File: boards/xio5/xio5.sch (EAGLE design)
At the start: 79 parts

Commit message: Start adding busses
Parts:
- removed U$1: ZTURN, pbxl:ZTURN
- added J1: 98424-G52-14ALF, samacsys:98424-G52-14ALF
- added JP1: (no value), pinhead:PINHD-1X7
- added ZTURN: ZTURN, pbxl:ZTURN
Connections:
- new net !SRST!: J1.B7, JP1.6, ZTURN-JTAG.!JTAG_RST!@CN1_14
- new net TCK: J1.B3, JP1.3, ZTURN-JTAG.JTAG_TCK@CN1_6
- new net TDI: J1.B5, JP1.5, ZTURN-JTAG.JTAG_TDI@CN1_10
- new net TDO: J1.B4, JP1.4, ZTURN-JTAG.JTAG_TDO@CN1_12
- new net TMS: J1.B2, JP1.2, ZTURN-JTAG.JTAG_TMS@CN1_8
- net +3V3: now also J1.B1, JP1.1, ZTURN-POWER.VDD33@CN1_3, ZTURN-POWER.VDD33@CN2_3, ZTURN-POWER.VDDIO_13_PL@CN1_15, ZTURN-POWER.VDDIO_34_PL@CN1_49, ZTURN-POWER.VDDIO_35_PL@CN2_51
- net +5V: now also ZTURN-POWER.VDD5@CN1_1, ZTURN-POWER.VDD5@CN2_1
- net GND: now also J1.A1, J1.A2, J1.A3, J1.A4, J1.A5, J1.A6, J1.A7, JP1.7, ZTURN-POWER.GND@CN1_2, ZTURN-POWER.GND@CN1_24, ZTURN-POWER.GND@CN1_25, ZTURN-POWER.GND@CN1_34, ZTURN-POWER.GND@CN1_35, ZTURN-POWER.GND@CN1_4, ZTURN-POWER.GND@CN1_44, ZTURN-POWER.GND@CN1_54, ZTURN-POWER.GND@CN1_67, ZTURN-POWER.GND@CN1_68, ZTURN-POWER.GND@CN2_2, ZTURN-POWER.GND@CN2_20, ZTURN-POWER.GND@CN2_21, ZTURN-POWER.GND@CN2_30, ZTURN-POWER.GND@CN2_31, ZTURN-POWER.GND@CN2_4, ZTURN-POWER.GND@CN2_40, ZTURN-POWER.GND@CN2_41, ZTURN-POWER.GND@CN2_50, ZTURN-POWER.GND@CN2_60, ZTURN-POWER.GND@CN2_61, ZTURN-POWER.GND@CN2_70, ZTURN-POWER.GND@CN2_71, ZTURN-POWER.GND@CN2_80
- net LO_A0: now also ZTURN-CN2.IO_B35_LN15@CN2_59
- net LO_A1: now also ZTURN-CN2.IO_B35_LP15@CN2_57
- net LO_A10: now also ZTURN-CN2.IO_B35_LN5@CN2_35
- net LO_A11: now also ZTURN-CN2.IO_B35_LP5@CN2_33
- net LO_A12: now also ZTURN-CN2.IO_B35_LN3@CN2_29
- net LO_A13: now also ZTURN-CN2.IO_B35_LP3@CN2_27
- net LO_A14: now also ZTURN-CN2.IO_B35_LN1@CN2_25
- net LO_A15: now also ZTURN-CN2.IO_B35_LP1@CN2_23
- net LO_A2: now also ZTURN-CN2.IO_B35_LN13@CN2_55
- net LO_A3: now also ZTURN-CN2.IO_B35_LP13@CN2_53
- net LO_A4: now also ZTURN-CN2.IO_B35_LN11@CN2_49
- net LO_A5: now also ZTURN-CN2.IO_B35_LP11@CN2_47
- net LO_A6: now also ZTURN-CN2.IO_B35_LN9@CN2_45
- net LO_A7: now also ZTURN-CN2.IO_B35_LP9@CN2_43
- net LO_A8: now also ZTURN-CN2.IO_B35_LN7@CN2_39
- net LO_A9: now also ZTURN-CN2.IO_B35_LP7@CN2_37
- net LO_D0: now also ZTURN-CN2.IO_B35_LN23@CN2_79
- net LO_D1: now also ZTURN-CN2.IO_B35_LP23@CN2_77
- net LO_D2: now also ZTURN-CN2.IO_B35_LN21@CN2_75
- net LO_D3: now also ZTURN-CN2.IO_B35_LP21@CN2_73
- net LO_D4: now also ZTURN-CN2.IO_B35_LN19@CN2_69
- net LO_D5: now also ZTURN-CN2.IO_B35_LP19@CN2_67
- net LO_D6: now also ZTURN-CN2.IO_B35_LN17@CN2_65
- net LO_D7: now also ZTURN-CN2.IO_B35_LP17@CN2_63
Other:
- note added: "Power, JTAG, unused"
- note removed: "SD Card"

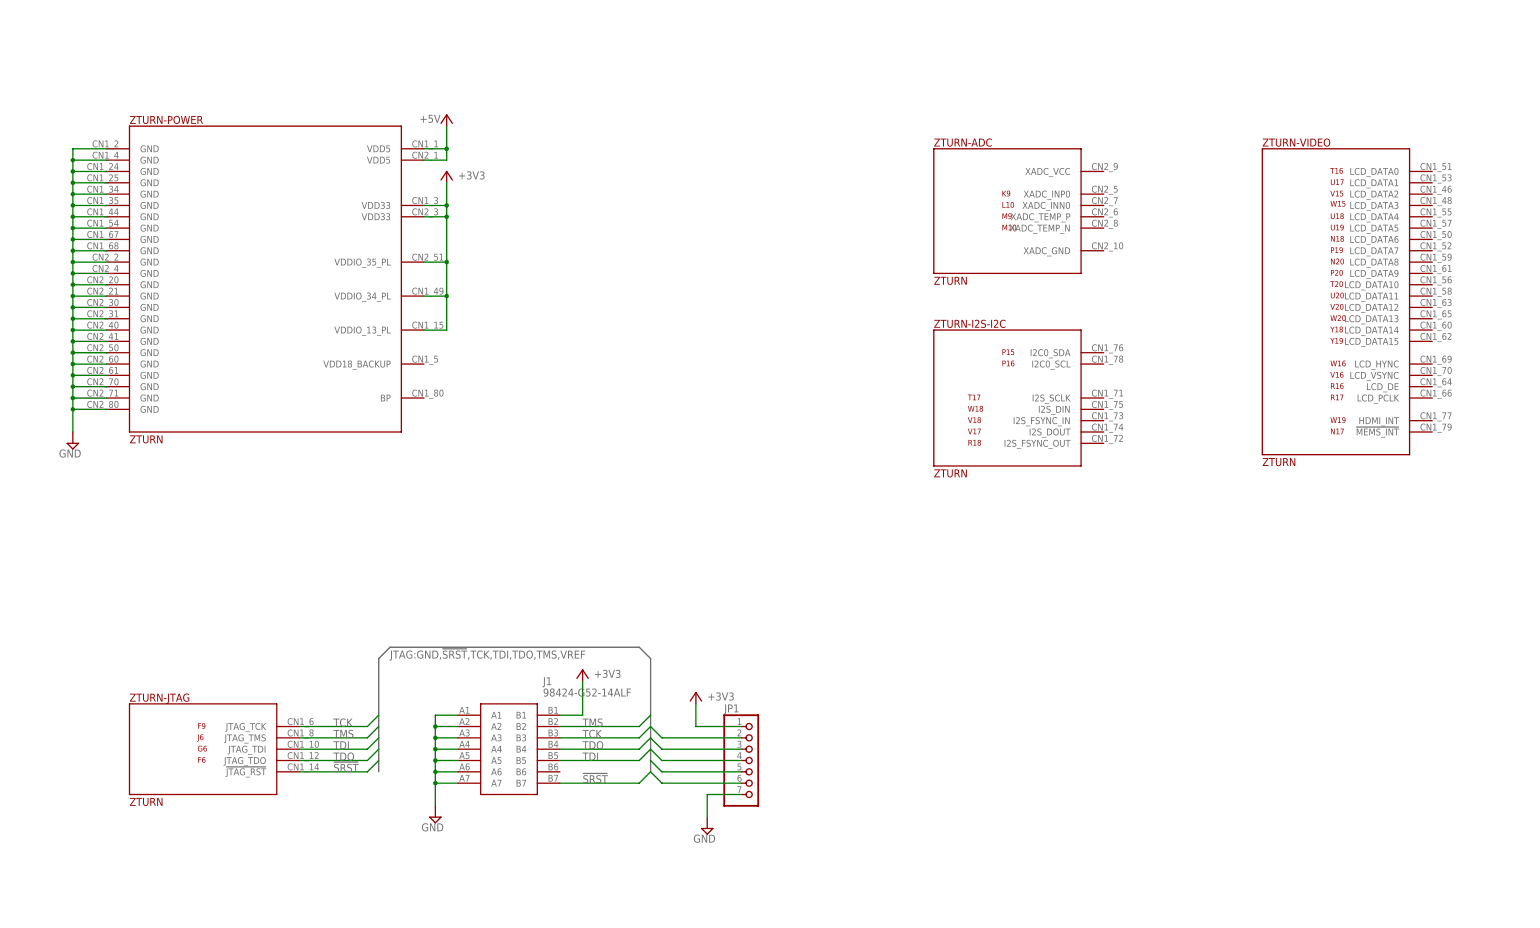
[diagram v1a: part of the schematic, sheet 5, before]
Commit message: Reorganise slot signals (ZBUS) and add the internal slot expansion interface (XBUS)
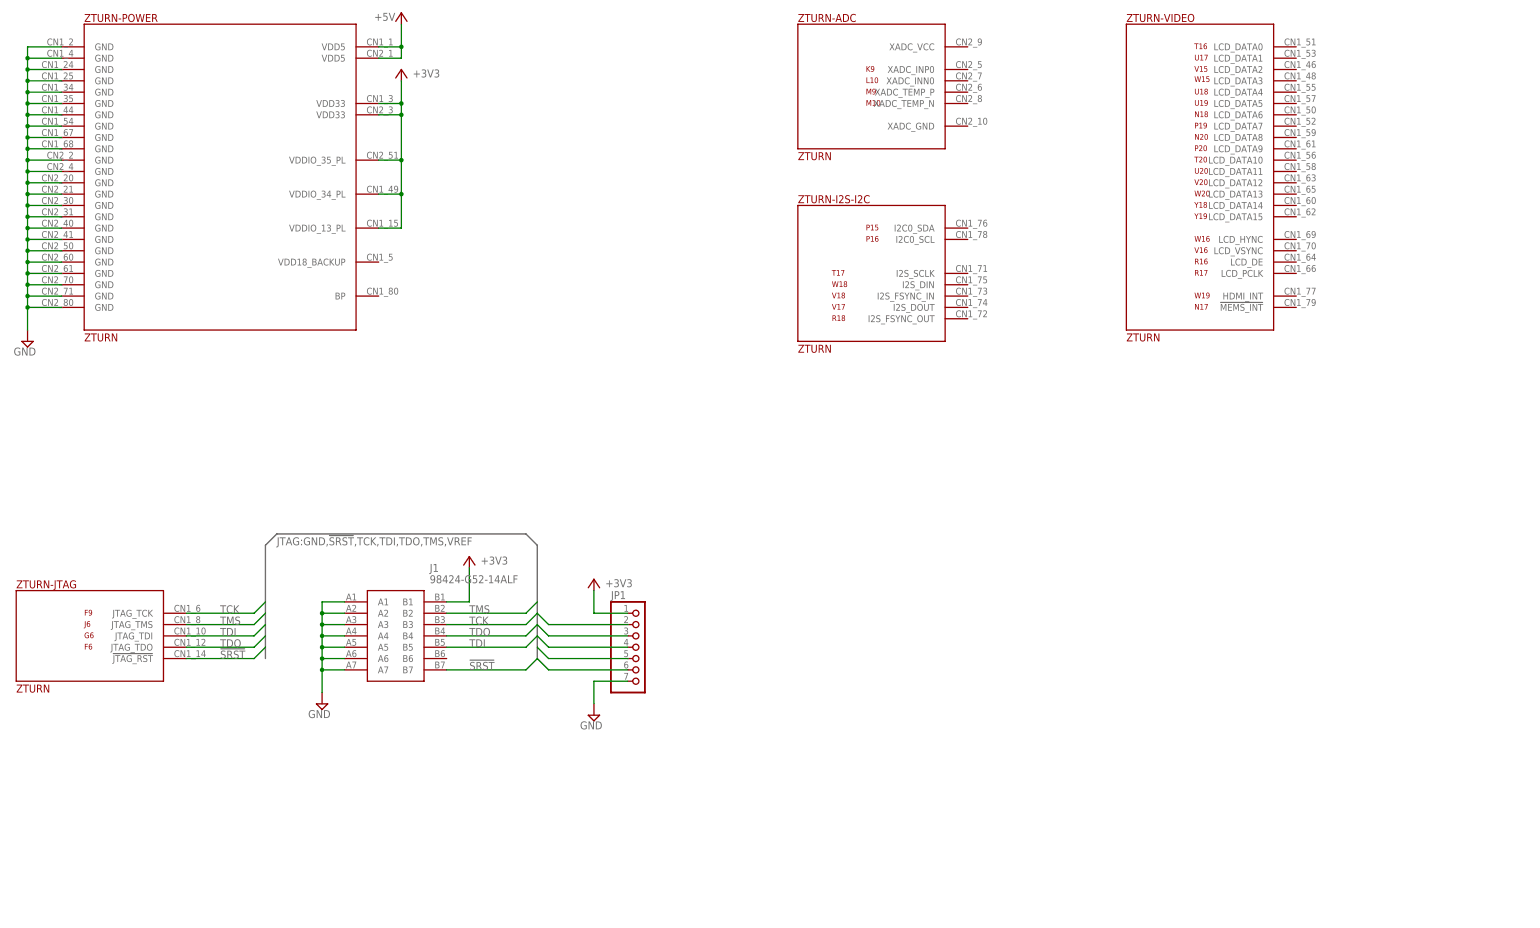
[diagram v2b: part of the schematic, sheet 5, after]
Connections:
- removed net !LO_CCTL!: SLOT0.A27, SLOT1.A27, SLOT2.A27, SLOT3.A27, SLOT4.A27
- removed net !LO_REF!: SLOT0.B15, SLOT1.B15, SLOT2.B15, SLOT3.B15, SLOT4.B15
- removed net HBUS0: SLOT0.B18, SLOT1.B18, SLOT2.B18, SLOT3.B18, SLOT4.B18
- removed net HBUS1: SLOT0.B19, SLOT1.B19, SLOT2.B19, SLOT3.B19, SLOT4.B19
- removed net HBUS10: SLOT0.B28, SLOT1.B28, SLOT2.B28, SLOT3.B28, SLOT4.B28
- removed net HBUS11: SLOT0.B29, SLOT1.B29, SLOT2.B29, SLOT3.B29, SLOT4.B29
- removed net HBUS12: SLOT0.B30, SLOT1.B30, SLOT2.B30, SLOT3.B30, SLOT4.B30
- removed net HBUS13: SLOT0.B31, SLOT1.B31, SLOT2.B31, SLOT3.B31, SLOT4.B31
- removed net HBUS2: SLOT0.B20, SLOT1.B20, SLOT2.B20, SLOT3.B20, SLOT4.B20
- removed net HBUS3: SLOT0.B21, SLOT1.B21, SLOT2.B21, SLOT3.B21, SLOT4.B21
- removed net HBUS4: SLOT0.B22, SLOT1.B22, SLOT2.B22, SLOT3.B22, SLOT4.B22
- removed net HBUS5: SLOT0.B23, SLOT1.B23, SLOT2.B23, SLOT3.B23, SLOT4.B23
- removed net HBUS6: SLOT0.B24, SLOT1.B24, SLOT2.B24, SLOT3.B24, SLOT4.B24
- removed net HBUS7: SLOT0.B25, SLOT1.B25, SLOT2.B25, SLOT3.B25, SLOT4.B25
- removed net HBUS8: SLOT0.B26, SLOT1.B26, SLOT2.B26, SLOT3.B26, SLOT4.B26
- removed net HBUS9: SLOT0.B27, SLOT1.B27, SLOT2.B27, SLOT3.B27, SLOT4.B27
- removed net SPI0_IRQ: SLOT0.A8
- removed net SPI0_MOSI: SLOT0.A9
- removed net SPI1_IRQ: SLOT1.A8
- removed net SPI1_MISO: SLOT1.A10
- removed net SPI1_MOSI: SLOT1.A9
- removed net SPI2_IRQ: SLOT2.A8
- removed net SPI2_MISO: SLOT2.A10
- removed net SPI2_MOSI: SLOT2.A9
- removed net SPI3_IRQ: SLOT3.A8
- removed net SPI3_MISO: SLOT3.A10
- removed net SPI3_MOSI: SLOT3.A9
- removed net SPI4_IRQ: SLOT4.A8
- removed net SPI4_MISO: SLOT4.A10
- removed net SPI4_MOSI: SLOT4.A9
- removed net SPIO_MISO: SLOT0.A10
- removed net VALID_RD: SLOT0.A7, SLOT1.A7, SLOT2.A7, SLOT3.A7, SLOT4.A7
- removed net VALID_WR: SLOT0.A6, SLOT1.A6, SLOT2.A6, SLOT3.A6, SLOT4.A6
- new net !AVALID!: SLOT0.A9, SLOT1.A9, SLOT2.A9, SLOT3.A9, SLOT4.A9
- new net HSPI0_IRQ0: SLOT0.A7, ZTURN-CN2.IO_B35_LN22@CN2_74
- new net HSPI0_IRQ1: SLOT1.A7, ZTURN-CN2.IO_B35_LP22@CN2_72
- new net HSPI0_IRQ2: SLOT2.A7, ZTURN-CN2.IO_B35_LN20@CN2_68
- new net HSPI0_MISO: SLOT0.A4, SLOT1.A4, SLOT2.A4, ZTURN-CN2.IO_B35_LN24@CN2_78
- new net HSPI0_MOSI: SLOT0.A5, SLOT1.A5, SLOT2.A5, ZTURN-CN2.IO_B35_LP24@CN2_76
- new net HSPI0_SS0: SLOT0.A6, ZTURN-CN2.IO_B35_LP20@CN2_66
- new net HSPI0_SS1: SLOT1.A6, ZTURN-CN2.IO_B35_LN18@CN2_64
- new net HSPI0_SS2: SLOT2.A6, ZTURN-CN2.IO_B35_LP18@CN2_62
- new net HSPI1_IRQ0: SLOT3.A7, ZTURN-CN2.IO_B35_LN14@CN2_54
- new net HSPI1_IRQ1: SLOT4.A7, ZTURN-CN2.IO_B35_LP14@CN2_52
- new net HSPI1_IRQ2: ZTURN-CN2.IO_B35_LN10@CN2_48
- new net HSPI1_MISO: SLOT3.A4, SLOT4.A4, ZTURN-CN2.IO_B35_LN16@CN2_58
- new net HSPI1_MOSI: SLOT3.A5, SLOT4.A5, ZTURN-CN2.IO_B35_LP16@CN2_56
- new net HSPI1_SS0: SLOT3.A6, ZTURN-CN2.IO_B35_LP12@CN2_46
- new net HSPI1_SS1: SLOT4.A6, ZTURN-CN2.IO_B35_LN10@CN2_44
- new net HSPI1_SS2: ZTURN-CN2.IO_B35_LP10@CN2_42
- new net SX_PRESENT: ZTURN-CN2.IO_B35_LP4@CN2_26
- new net XBUS0: ZTURN-CN1.IO_B34_LP11@CN1_45
- new net XBUS1: ZTURN-CN1.IO_B34_LN11@CN1_47
- new net XBUS10: ZTURN-CN1.IO_B34_LP5@CN1_36
- new net XBUS11: ZTURN-CN1.IO_B34_LN5@CN1_38
- new net XBUS12: ZTURN-CN1.IO_B34_LP7@CN1_40
- new net XBUS13: ZTURN-CN1.IO_B34_LN7@CN1_42
- new net XBUS14: ZTURN-CN2.IO_B35_LP2@CN2_22
- new net XBUS15: ZTURN-CN2.IO_B35_LN2@CN2_24
- new net XBUS2: ZTURN-CN1.IO_B13_LP14@CN1_16
- new net XBUS3: ZTURN-CN1.IO_B13_LN14@CN1_18
- new net XBUS4: ZTURN-CN1.IO_B13_LP21@CN1_20
- new net XBUS5: ZTURN-CN1.IO_B13_LN21@CN1_22
- new net XBUS6: ZTURN-CN1.IO_B34_LP1@CN1_26
- new net XBUS7: ZTURN-CN1.IO_B34_LN1@CN1_28
- new net XBUS8: ZTURN-CN1.IO_B34_LP3@CN1_30
- new net XBUS9: ZTURN-CN1.IO_B34_LN3@CN1_32
- new net ZBUS0: SLOT0.B16, SLOT1.B16, SLOT2.B16, SLOT3.B16, SLOT4.B16, ZTURN-CN1.IO_B34_LN8@CN1_43
- new net ZBUS1: SLOT0.B17, SLOT1.B17, SLOT2.B17, SLOT3.B17, SLOT4.B17, ZTURN-CN1.IO_B34_LP8@CN1_41
- new net ZBUS10: SLOT0.B26, SLOT1.B26, SLOT2.B26, SLOT3.B26, SLOT4.B26, ZTURN-CN1.IO_B13_LN13@CN1_19
- new net ZBUS11: SLOT0.B27, SLOT1.B27, SLOT2.B27, SLOT3.B27, SLOT4.B27, ZTURN-CN1.IO_B13_LP13@CN1_17
- new net ZBUS12: SLOT0.B28, SLOT1.B28, SLOT2.B28, SLOT3.B28, SLOT4.B28, ZTURN-CN1.IO_B13_LN12@CN1_13
- new net ZBUS13: SLOT0.B29, SLOT1.B29, SLOT2.B29, SLOT3.B29, SLOT4.B29, ZTURN-CN1.IO_B13_P12@CN1_11
- new net ZBUS14: SLOT0.B30, SLOT1.B30, SLOT2.B30, SLOT3.B30, SLOT4.B30, ZTURN-CN1.IO_B13_LN11@CN1_9
- new net ZBUS15: SLOT0.B31, SLOT1.B31, SLOT2.B31, SLOT3.B31, SLOT4.B31, ZTURN-CN1.IO_B13_LP11@CN1_7
- new net ZBUS2: SLOT0.B18, SLOT1.B18, SLOT2.B18, SLOT3.B18, SLOT4.B18, ZTURN-CN1.IO_B34_LN6@CN1_39
- new net ZBUS3: SLOT0.B19, SLOT1.B19, SLOT2.B19, SLOT3.B19, SLOT4.B19, ZTURN-CN1.IO_B34_LP6@CN1_37
- new net ZBUS4: SLOT0.B20, SLOT1.B20, SLOT2.B20, SLOT3.B20, SLOT4.B20, ZTURN-CN1.IO_B34_LN4@CN1_33
- new net ZBUS5: SLOT0.B21, SLOT1.B21, SLOT2.B21, SLOT3.B21, SLOT4.B21, ZTURN-CN1.IO_B34_LP4@CN1_31
- new net ZBUS6: SLOT0.B22, SLOT1.B22, SLOT2.B22, SLOT3.B22, SLOT4.B22, ZTURN-CN1.IO_B34_LN2@CN1_29
- new net ZBUS7: SLOT0.B23, SLOT1.B23, SLOT2.B23, SLOT3.B23, SLOT4.B23, ZTURN-CN1.IO_B34_LP2@CN1_27
- new net ZBUS8: SLOT0.B24, SLOT1.B24, SLOT2.B24, SLOT3.B24, SLOT4.B24, ZTURN-CN1.IO_B13_LN15@CN1_23
- new net ZBUS9: SLOT0.B25, SLOT1.B25, SLOT2.B25, SLOT3.B25, SLOT4.B25, ZTURN-CN1.IO_B13_LP15@CN1_21
- net !LO_RST!: now also SLOT0.A27, SLOT1.A27, SLOT2.A27, SLOT3.A27, SLOT4.A27; no longer SLOT0.B16, SLOT1.B16, SLOT2.B16, SLOT3.B16, SLOT4.B16
- net GND: now also SLOT0.A10, SLOT0.A8, SLOT1.A10, SLOT1.A8, SLOT2.A10, SLOT2.A8, SLOT3.A10, SLOT3.A8, SLOT4.A10, SLOT4.A8; no longer SLOT0.A4, SLOT0.A5, SLOT1.A4, SLOT1.A5, SLOT2.A4, SLOT2.A5, SLOT3.A4, SLOT3.A5, SLOT4.A4, SLOT4.A5
- net LO_A10: now also ZTURN-CN2.IO_B35_LP3@CN2_27; no longer ZTURN-CN2.IO_B35_LN5@CN2_35
- net LO_A11: now also ZTURN-CN2.IO_B35_LN3@CN2_29; no longer ZTURN-CN2.IO_B35_LP5@CN2_33
- net LO_A12: now also ZTURN-CN2.IO_B35_LP5@CN2_33; no longer ZTURN-CN2.IO_B35_LN3@CN2_29
- net LO_A13: now also ZTURN-CN2.IO_B35_LN5@CN2_35; no longer ZTURN-CN2.IO_B35_LP3@CN2_27
- net LO_A14: now also ZTURN-CN2.IO_B35_LP7@CN2_37; no longer ZTURN-CN2.IO_B35_LN1@CN2_25
- net LO_A15: now also ZTURN-CN2.IO_B35_LN7@CN2_39; no longer ZTURN-CN2.IO_B35_LP1@CN2_23
- net LO_A8: now also ZTURN-CN2.IO_B35_LP1@CN2_23; no longer ZTURN-CN2.IO_B35_LN7@CN2_39
- net LO_A9: now also ZTURN-CN2.IO_B35_LN1@CN2_25; no longer ZTURN-CN2.IO_B35_LP7@CN2_37
- net LO_R/!W!: now also SLOT0.B15, SLOT1.B15, SLOT2.B15, SLOT3.B15, SLOT4.B15; no longer SLOT0.B17, SLOT1.B17, SLOT2.B17, SLOT3.B17, SLOT4.B17
- net S0_PRESENT: now also ZTURN-CN2.IO_B35_LN8@CN2_38
- net S1_PRESENT: now also ZTURN-CN2.IO_B35_LP8@CN2_36
- net S2_PRESENT: now also ZTURN-CN2.IO_B35_LN6@CN2_34
- net S3_PRESENT: now also ZTURN-CN2.IO_B35_LP6@CN2_32
- net S4_PRESENT: now also ZTURN-CN2.IO_B35_LN4@CN2_28
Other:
- note added: "!ADDR_VALID!"
- note added: "!PRESENT! x5"
- note added: "Zynq 7020 CGA400"
- note removed: "!ADDR_VALID_READ!"
- note removed: "!ADDR_VALID_WRITE!"
- note removed: "/7"
- note removed: "Artix 7 XC7A35T-1 BGA256"
- moved on the sheet: C55, J1, JP1, LD_2P, R101, R63, SLOT2, ZTURN-ADC, ZTURN-I2S-I2C, ZTURN-JTAG, ZTURN-POWER, ZTURN-VIDEO

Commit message: Work on some of the internal expansion stuff
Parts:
- added C19: 0.1uF, rcl:C-EUC0201
- added IC1: PCAL6416APW,118, samacsys:PCAL6416APW,118
- added JP2: (no value), pinhead:PINHD-2X2
- added JP3: (no value), pinhead-2:PINHD-2X16_2.00
- added LD_M0, LD_M1: Orange, led:LEDCHIPLED_0603
- added R1, R6: 59R, rcl:R-EU_R0402
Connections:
- removed net XBUS0: ZTURN-CN1.IO_B34_LP11@CN1_45
- removed net XBUS1: ZTURN-CN1.IO_B34_LN11@CN1_47
- removed net XBUS10: ZTURN-CN1.IO_B34_LP5@CN1_36
- removed net XBUS11: ZTURN-CN1.IO_B34_LN5@CN1_38
- removed net XBUS12: ZTURN-CN1.IO_B34_LP7@CN1_40
- removed net XBUS13: ZTURN-CN1.IO_B34_LN7@CN1_42
- removed net XBUS14: ZTURN-CN2.IO_B35_LP2@CN2_22
- removed net XBUS15: ZTURN-CN2.IO_B35_LN2@CN2_24
- removed net XBUS2: ZTURN-CN1.IO_B13_LP14@CN1_16
- removed net XBUS3: ZTURN-CN1.IO_B13_LN14@CN1_18
- removed net XBUS4: ZTURN-CN1.IO_B13_LP21@CN1_20
- removed net XBUS5: ZTURN-CN1.IO_B13_LN21@CN1_22
- removed net XBUS6: ZTURN-CN1.IO_B34_LP1@CN1_26
- removed net XBUS7: ZTURN-CN1.IO_B34_LN1@CN1_28
- removed net XBUS8: ZTURN-CN1.IO_B34_LP3@CN1_30
- removed net XBUS9: ZTURN-CN1.IO_B34_LN3@CN1_32
- new net N$2: IC1.P0_7, R6.2
- new net N$3: LD_M1.A, R6.1
- new net N$4: IC1.!INT, ZTURN-CN2.IO_B35_LP8@CN2_36
- new net N$5: IC1.!RESET, ZTURN-CN2.IO_B35_LN8@CN2_38
- new net N$7: IC1.P0_6, R1.2
- new net N$8: LD_M0.A, R1.1
- new net SCL: IC1.SCL, JP2.2, ZTURN-I2S-I2C.I2C0_SCL@CN1_78
- new net SDA: IC1.SDA, JP2.4, ZTURN-I2S-I2C.I2C0_SDA@CN1_76
- new net XIO0: IC1.P1_0, JP3.13
- new net XIO1: IC1.P1_1, JP3.15
- new net XIO2: IC1.P1_2, JP3.17
- new net XIO3: IC1.P1_3, JP3.19
- new net XIO4: IC1.P1_4, JP3.21
- new net XIO5: IC1.P1_5, JP3.23
- new net XIO6: IC1.P1_6, JP3.25
- new net XIO7: IC1.P1_7, JP3.27
- new net XSPI_IRQ: JP3.5, ZTURN-CN2.IO_B35_LN4@CN2_28
- new net XSPI_MISO: JP2.1, JP3.7, ZTURN-CN2.IO_B35_LP6@CN2_32
- new net XSPI_MOSI: JP2.3, JP3.9, ZTURN-CN2.IO_B35_LN6@CN2_34
- net !LO_EXTSEL!: now also ZTURN-CN1.IO_B34_LN3@CN1_32
- net !LO_HALT!: now also ZTURN-CN1.IO_B34_LP5@CN1_36
- net !LO_IRQ!: now also ZTURN-CN1.IO_B34_LN5@CN1_38
- net !LO_MPD!: now also ZTURN-CN1.IO_B34_LP7@CN1_40
- net !LO_RST!: now also ZTURN-CN2.IO_B35_LN2@CN2_24
- net +3V3: now also C19.1, IC1.VDD(I2C-BUS), IC1.VDD(P)
- net +5V: now also JP3.1, JP3.3
- net DIR_A: now also ZTURN-CN1.IO_B34_LP11@CN1_45
- net DIR_CLK: no longer U$15.DIR@5
- net DIR_D: now also ZTURN-CN1.IO_B34_LN11@CN1_47
- net DIR_EXTSEL: now also ZTURN-CN1.IO_B13_LP14@CN1_16
- net DIR_HALT: now also ZTURN-CN1.IO_B13_LN14@CN1_18
- net DIR_IRQ: now also ZTURN-CN1.IO_B13_LP21@CN1_20
- net DIR_MPD: now also ZTURN-CN1.IO_B13_LN21@CN1_22
- net DIR_RD4: no longer U$16.DIR@5
- net DIR_RD5: no longer U$14.DIR@5
- net DIR_RST: now also ZTURN-CN1.IO_B34_LP1@CN1_26
- net DIR_RW: now also ZTURN-CN1.IO_B34_LN1@CN1_28
- net GND: now also C19.2, IC1.ADDR, IC1.VSS, JP3.29, JP3.31, LD_M0.C, LD_M1.C, U$14.DIR@5, U$15.DIR@5, U$16.DIR@5
- net LO_CLK: now also ZTURN-CN1.IO_B34_LP3@CN1_30
- net LO_R/!W!: now also ZTURN-CN2.IO_B35_LP4@CN2_26
- net LO_RD4: now also ZTURN-CN1.IO_B34_LN7@CN1_42
- net LO_RD5: now also ZTURN-CN2.IO_B35_LP2@CN2_22
- net S0_PRESENT: now also IC1.P0_0; no longer ZTURN-CN2.IO_B35_LN8@CN2_38
- net S1_PRESENT: now also IC1.P0_1; no longer ZTURN-CN2.IO_B35_LP8@CN2_36
- net S2_PRESENT: now also IC1.P0_2; no longer ZTURN-CN2.IO_B35_LN6@CN2_34
- net S3_PRESENT: now also IC1.P0_3; no longer ZTURN-CN2.IO_B35_LP6@CN2_32
- net S4_PRESENT: now also IC1.P0_4; no longer ZTURN-CN2.IO_B35_LN4@CN2_28
- net SX_PRESENT: now also IC1.P0_5, JP3.11; no longer ZTURN-CN2.IO_B35_LP4@CN2_26
- net ZBUS0: now also JP3.32
- net ZBUS1: now also JP3.30
- net ZBUS10: now also JP3.12
- net ZBUS11: now also JP3.10
- net ZBUS12: now also JP3.8
- net ZBUS13: now also JP3.6
- net ZBUS14: now also JP3.4
- net ZBUS15: now also JP3.2
- net ZBUS2: now also JP3.28
- net ZBUS3: now also JP3.26
- net ZBUS4: now also JP3.24
- net ZBUS5: now also JP3.22
- net ZBUS6: now also JP3.20
- net ZBUS7: now also JP3.18
- net ZBUS8: now also JP3.16
- net ZBUS9: now also JP3.14
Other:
- moved on the sheet: ZTURN-CN1, ZTURN-CN2
